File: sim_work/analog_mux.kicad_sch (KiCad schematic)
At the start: 4 parts, among them U1 MAX338, U2 MAX338

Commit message: Per-block PDF schematics: 6 oscillator + 6 TIA blocks with merged PDFs
Add individual A4 schematic generation for each functional circuit block:
- Oscillator: summing amp, integrator 1/2, RMS detector, power supply, MCU
- TIA: input filters, analog mux, mux TIA, relay ladder, MCU section, electrometer
- merge_pdfs() helper using PyMuPDF for multi-page output
- CLI commands: osc_blocks, tia_blocks
- All blocks verified: 0 wire crossings, complete pin connectivity

Co-Authored-By: Claude Opus 4.6 <noreply@anthropic.com>
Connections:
- net 3V3 renamed VCC
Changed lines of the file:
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@@
 		(instances
 			(project "Analog Multiplexer - 2x MAX338 (CD4051B)"
-				(path "/1a12a359-40ac-4b10-9e74-02d138511f5c"
+				(path "/cf5c95e5-da59-4127-8934-74012ff3903c"
 					(reference "U1")
 					(unit 1)
@@
 			)
 		)
-		(property "Value" "3V3"
+		(property "Value" "VCC"
 			(at 104.14 51.816 0.0000)
 			(effects
@@
 		(instances
 			(project "Analog Multiplexer - 2x MAX338 (CD4051B)"
-				(path "/1a12a359-40ac-4b10-9e74-02d138511f5c"
+				(path "/cf5c95e5-da59-4127-8934-74012ff3903c"
 					(reference "#PWR001")
 					(unit 1)
@@
 		(instances
 			(project "Analog Multiplexer - 2x MAX338 (CD4051B)"
-				(path "/1a12a359-40ac-4b10-9e74-02d138511f5c"
+				(path "/cf5c95e5-da59-4127-8934-74012ff3903c"
 					(reference "#PWR002")
 					(unit 1)
@@
 		(instances
 			(project "Analog Multiplexer - 2x MAX338 (CD4051B)"
-				(path "/1a12a359-40ac-4b10-9e74-02d138511f5c"
+				(path "/cf5c95e5-da59-4127-8934-74012ff3903c"
 					(reference "#PWR003")
 					(unit 1)
@@
 		(instances
 			(project "Analog Multiplexer - 2x MAX338 (CD4051B)"
-				(path "/1a12a359-40ac-4b10-9e74-02d138511f5c"
+				(path "/cf5c95e5-da59-4127-8934-74012ff3903c"
 					(reference "C17")
 					(unit 1)
@@
 		(instances
 			(project "Analog Multiplexer - 2x MAX338 (CD4051B)"
-				(path "/1a12a359-40ac-4b10-9e74-02d138511f5c"
+				(path "/cf5c95e5-da59-4127-8934-74012ff3903c"
 					(reference "#PWR004")
 					(unit 1)
@@
 		(instances
 			(project "Analog Multiplexer - 2x MAX338 (CD4051B)"
-				(path "/1a12a359-40ac-4b10-9e74-02d138511f5c"
+				(path "/cf5c95e5-da59-4127-8934-74012ff3903c"
 					(reference "U2")
 					(unit 1)
@@
 			)
 		)
-		(property "Value" "3V3"
+		(property "Value" "VCC"
 			(at 104.14 153.416 0.0000)
 			(effects
@@
 		(instances
 			(project "Analog Multiplexer - 2x MAX338 (CD4051B)"
-				(path "/1a12a359-40ac-4b10-9e74-02d138511f5c"
+				(path "/cf5c95e5-da59-4127-8934-74012ff3903c"
 					(reference "#PWR005")
 					(unit 1)
@@
 		(instances
 			(project "Analog Multiplexer - 2x MAX338 (CD4051B)"
-				(path "/1a12a359-40ac-4b10-9e74-02d138511f5c"
+				(path "/cf5c95e5-da59-4127-8934-74012ff3903c"
 					(reference "#PWR006")
 					(unit 1)
@@
 		(instances
 			(project "Analog Multiplexer - 2x MAX338 (CD4051B)"
-				(path "/1a12a359-40ac-4b10-9e74-02d138511f5c"
+				(path "/cf5c95e5-da59-4127-8934-74012ff3903c"
 					(reference "#PWR007")
 					(unit 1)
@@
 		(instances
 			(project "Analog Multiplexer - 2x MAX338 (CD4051B)"
-				(path "/1a12a359-40ac-4b10-9e74-02d138511f5c"
+				(path "/cf5c95e5-da59-4127-8934-74012ff3903c"
 					(reference "C18")
 					(unit 1)
@@
 		(instances
 			(project "Analog Multiplexer - 2x MAX338 (CD4051B)"
-				(path "/1a12a359-40ac-4b10-9e74-02d138511f5c"
+				(path "/cf5c95e5-da59-4127-8934-74012ff3903c"
 					(reference "#PWR008")
 					(unit 1)

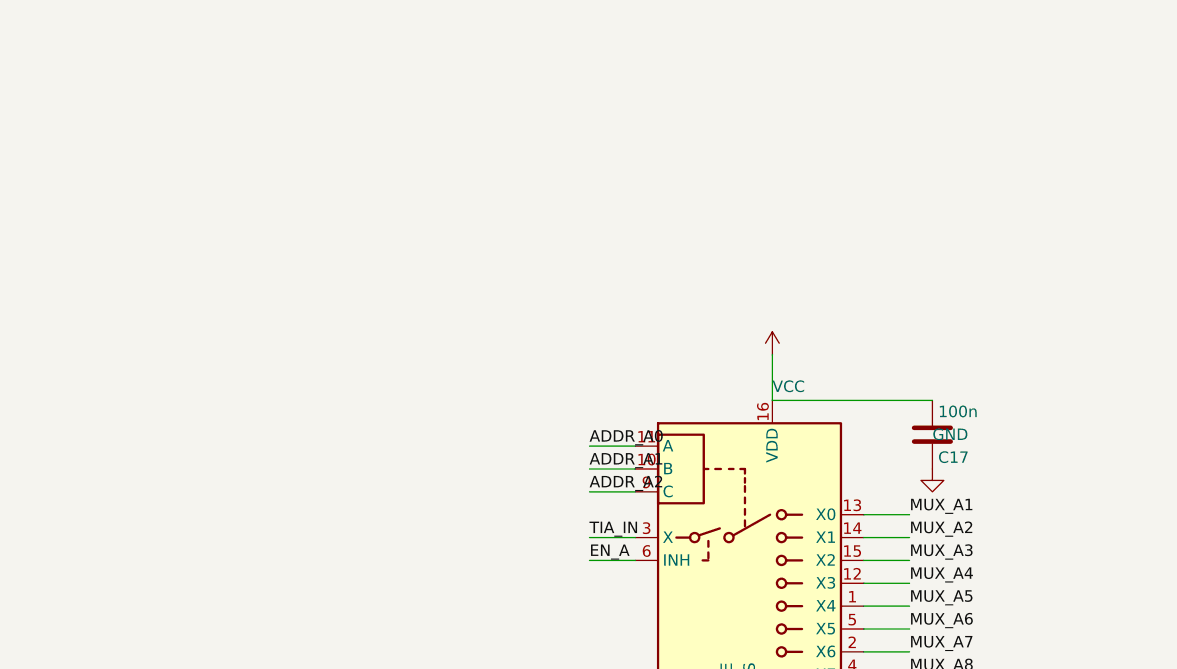
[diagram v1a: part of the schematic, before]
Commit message: Fix schematic connections, add docs and repo portability
- Input filters: R rotation=90 (horizontal), ESD diode rotations fixed,
  junction dots at cathode-signal connection, wires to GND symbols
- Relay ladder: flyback diode rotation 270->90 (K top, A bottom)
- Electrometer/Mux TIA: 4 junction dots each at T-junctions
- AD636 RMS detector: proper IC box with pin labels replaces text-only
- Oscillator blocks: D_Zener symbol, L-shaped cathode routing
- TIA blocks: title/function annotations on all 5 blocks
- New: requirements.txt, docs/oscillator_guide.md
- D_Zener.kicad_sym added to bundled symbols/
- .gitignore updated for docs/ and requirements.txt
- README updated with pip install -r requirements.txt
- PROJECT.md session 9 changelog
- SimGUI builds clean (0 errors)

Co-Authored-By: Claude Opus 4.6 <noreply@anthropic.com>
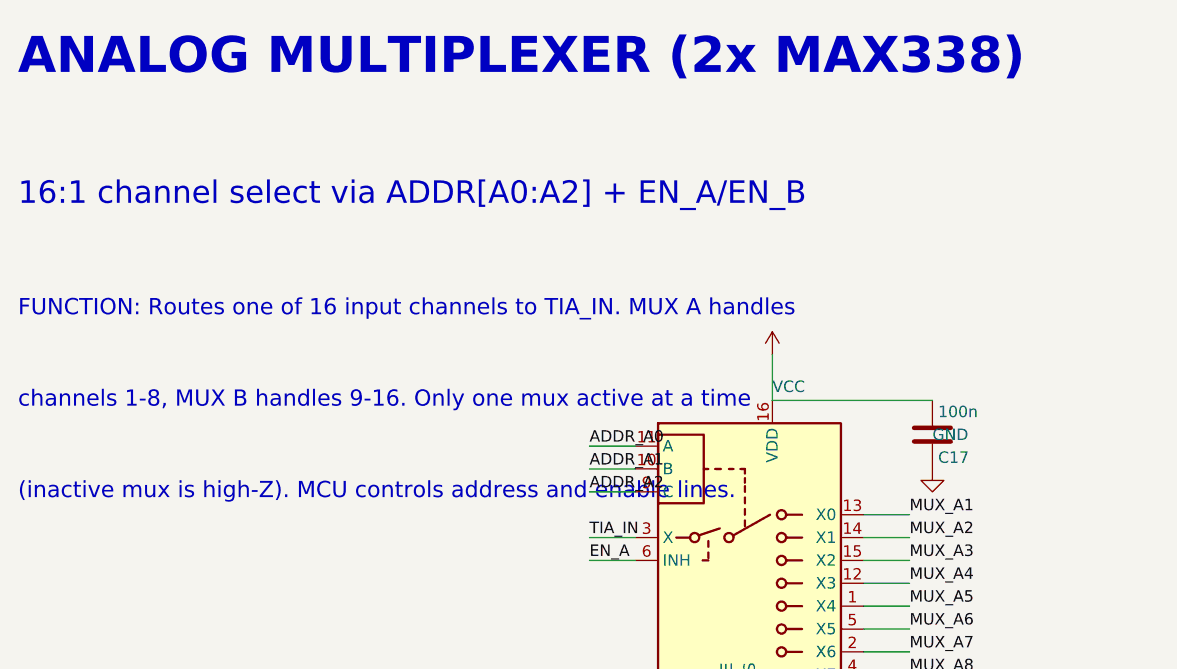
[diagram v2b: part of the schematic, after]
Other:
- note added: "(inactive mux is high-Z). MCU controls address and enable lines."
- note added: "16:1 channel select via ADDR[A0:A2] + EN_A/EN_B"
- note added: "ANALOG MULTIPLEXER (2x MAX338)"
- note added: "FUNCTION: Routes one of 16 input channels to TIA_IN. MUX A handles"
- note added: "channels 1-8, MUX B handles 9-16. Only one mux active at a time"
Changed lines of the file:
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@@
 		(instances
 			(project "Analog Multiplexer - 2x MAX338 (CD4051B)"
-				(path "/cf5c95e5-da59-4127-8934-74012ff3903c"
+				(path "/61d22642-77f1-437a-a40a-3840d0f0dcf6"
 					(reference "U1")
 					(unit 1)
@@
 		(instances
 			(project "Analog Multiplexer - 2x MAX338 (CD4051B)"
-				(path "/cf5c95e5-da59-4127-8934-74012ff3903c"
+				(path "/61d22642-77f1-437a-a40a-3840d0f0dcf6"
 					(reference "#PWR001")
 					(unit 1)
@@
 		(instances
 			(project "Analog Multiplexer - 2x MAX338 (CD4051B)"
-				(path "/cf5c95e5-da59-4127-8934-74012ff3903c"
+				(path "/61d22642-77f1-437a-a40a-3840d0f0dcf6"
 					(reference "#PWR002")
 					(unit 1)
@@
 		(instances
 			(project "Analog Multiplexer - 2x MAX338 (CD4051B)"
-				(path "/cf5c95e5-da59-4127-8934-74012ff3903c"
+				(path "/61d22642-77f1-437a-a40a-3840d0f0dcf6"
 					(reference "#PWR003")
 					(unit 1)
@@
 		(instances
 			(project "Analog Multiplexer - 2x MAX338 (CD4051B)"
-				(path "/cf5c95e5-da59-4127-8934-74012ff3903c"
+				(path "/61d22642-77f1-437a-a40a-3840d0f0dcf6"
 					(reference "C17")
 					(unit 1)
@@
 		(instances
 			(project "Analog Multiplexer - 2x MAX338 (CD4051B)"
-				(path "/cf5c95e5-da59-4127-8934-74012ff3903c"
+				(path "/61d22642-77f1-437a-a40a-3840d0f0dcf6"
 					(reference "#PWR004")
 					(unit 1)
@@
 		(instances
 			(project "Analog Multiplexer - 2x MAX338 (CD4051B)"
-				(path "/cf5c95e5-da59-4127-8934-74012ff3903c"
+				(path "/61d22642-77f1-437a-a40a-3840d0f0dcf6"
 					(reference "U2")
 					(unit 1)
@@
 		(instances
 			(project "Analog Multiplexer - 2x MAX338 (CD4051B)"
-				(path "/cf5c95e5-da59-4127-8934-74012ff3903c"
+				(path "/61d22642-77f1-437a-a40a-3840d0f0dcf6"
 					(reference "#PWR005")
 					(unit 1)
@@
 		(instances
 			(project "Analog Multiplexer - 2x MAX338 (CD4051B)"
-				(path "/cf5c95e5-da59-4127-8934-74012ff3903c"
+				(path "/61d22642-77f1-437a-a40a-3840d0f0dcf6"
 					(reference "#PWR006")
 					(unit 1)
@@
 		(instances
 			(project "Analog Multiplexer - 2x MAX338 (CD4051B)"
-				(path "/cf5c95e5-da59-4127-8934-74012ff3903c"
+				(path "/61d22642-77f1-437a-a40a-3840d0f0dcf6"
 					(reference "#PWR007")
 					(unit 1)
@@
 		(instances
 			(project "Analog Multiplexer - 2x MAX338 (CD4051B)"
-				(path "/cf5c95e5-da59-4127-8934-74012ff3903c"
+				(path "/61d22642-77f1-437a-a40a-3840d0f0dcf6"
 					(reference "C18")
 					(unit 1)
@@
 		(instances
 			(project "Analog Multiplexer - 2x MAX338 (CD4051B)"
-				(path "/cf5c95e5-da59-4127-8934-74012ff3903c"
+				(path "/61d22642-77f1-437a-a40a-3840d0f0dcf6"
 					(reference "#PWR008")
 					(unit 1)
@@
 		)
 	)
+	(text "ANALOG MULTIPLEXER (2x MAX338)"
+		(exclude_from_sim no)
+		(at 20.32 15.24 0.0000)
+		(effects
+			(font
+				(size 4 4)
+				(bold yes)
+			)
+			(justify left)
+		)
+	)
+	(text "16:1 channel select via ADDR[A0:A2] + EN_A/EN_B"
+		(exclude_from_sim no)
+		(at 20.32 30.48 0.0000)
+		(effects
+			(font
+				(size 2.5 2.5)
+			)
+			(justify left)
+		)
+	)
+	(text "FUNCTION: Routes one of 16 input channels to TIA_IN. MUX A handles"
+		(exclude_from_sim no)
+		(at 20.32 43.18 0.0000)
+		(effects
+			(font
+				(size 1.8 1.8)
+			)
+			(justify left)
+		)
+	)
+	(text "channels 1-8, MUX B handles 9-16. Only one mux active at a time"
+		(exclude_from_sim no)
+		(at 20.32 53.34 0.0000)
+		(effects
+			(font
+				(size 1.8 1.8)
+			)
+			(justify left)
+		)
+	)
+	(text "(inactive mux is high-Z). MCU controls address and enable lines."
+		(exclude_from_sim no)
+		(at 20.32 63.5 0.0000)
+		(effects
+			(font
+				(size 1.8 1.8)
+			)
+			(justify left)
+		)
+	)
